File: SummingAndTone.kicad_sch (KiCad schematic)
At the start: 9 parts, among them U2 TL072

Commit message: using smt caps and resistors
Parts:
- C14, C15: footprint ECE319K:C_Axial_200mil -> Capacitor_SMD:C_0805_2012Metric_Pad1.18x1.45mm_HandSolder
- R19, R20, R21, R22, R23: footprint Resistor_THT:R_Axial_DIN0207_L6.3mm_D2.5mm_P10.16mm_Horizontal -> Resistor_SMD:R_0805_2012Metric_Pad1.20x1.40mm_HandSolder
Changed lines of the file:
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@@
 			)
 		)
-		(property "Footprint" "Resistor_THT:R_Axial_DIN0207_L6.3mm_D2.5mm_P10.16mm_Horizontal"
+		(property "Footprint" "Resistor_SMD:R_0805_2012Metric_Pad1.20x1.40mm_HandSolder"
 			(at 133.223 106.68 90)
 			(effects
@@
 			)
 		)
-		(property "Footprint" "Resistor_THT:R_Axial_DIN0207_L6.3mm_D2.5mm_P10.16mm_Horizontal"
+		(property "Footprint" "Resistor_SMD:R_0805_2012Metric_Pad1.20x1.40mm_HandSolder"
 			(at 155.575 121.158 90)
 			(effects
@@
 			)
 		)
-		(property "Footprint" "ECE319K:C_Axial_200mil"
+		(property "Footprint" "Capacitor_SMD:C_0805_2012Metric_Pad1.18x1.45mm_HandSolder"
 			(at 144.78 118.4148 0)
 			(effects
@@
 			)
 		)
-		(property "Footprint" "ECE319K:C_Axial_200mil"
+		(property "Footprint" "Capacitor_SMD:C_0805_2012Metric_Pad1.18x1.45mm_HandSolder"
 			(at 113.665 119.6848 0)
 			(effects
@@
 			)
 		)
-		(property "Footprint" "Resistor_THT:R_Axial_DIN0207_L6.3mm_D2.5mm_P10.16mm_Horizontal"
+		(property "Footprint" "Resistor_SMD:R_0805_2012Metric_Pad1.20x1.40mm_HandSolder"
 			(at 155.575 130.683 90)
 			(effects
@@
 			)
 		)
-		(property "Footprint" "Resistor_THT:R_Axial_DIN0207_L6.3mm_D2.5mm_P10.16mm_Horizontal"
+		(property "Footprint" "Resistor_SMD:R_0805_2012Metric_Pad1.20x1.40mm_HandSolder"
 			(at 139.7 98.933 90)
 			(effects
@@
 			)
 		)
-		(property "Footprint" "Resistor_THT:R_Axial_DIN0207_L6.3mm_D2.5mm_P10.16mm_Horizontal"
+		(property "Footprint" "Resistor_SMD:R_0805_2012Metric_Pad1.20x1.40mm_HandSolder"
 			(at 109.855 111.633 90)
 			(effects

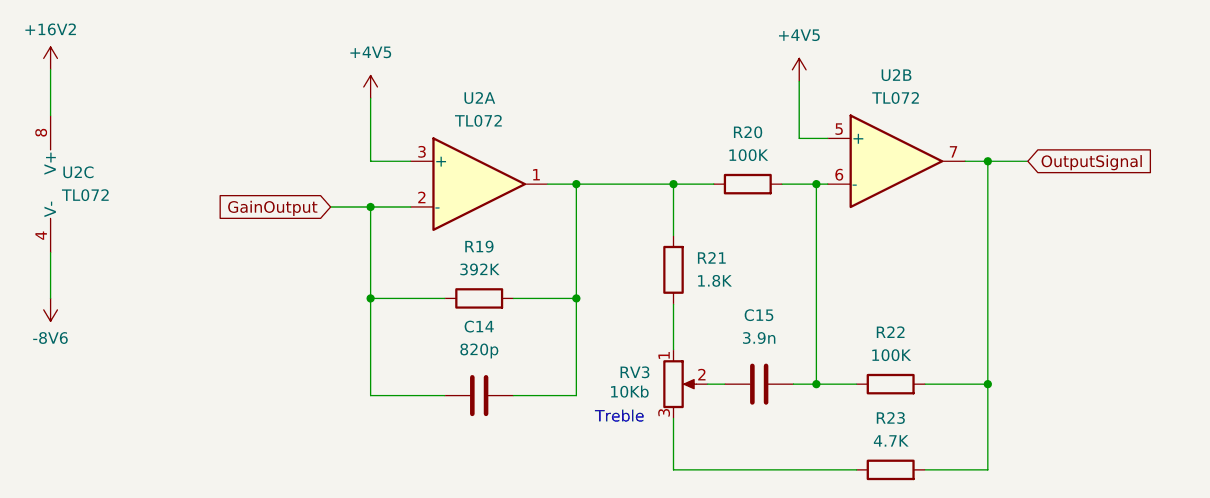
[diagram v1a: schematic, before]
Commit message: change metal film resistor footprint
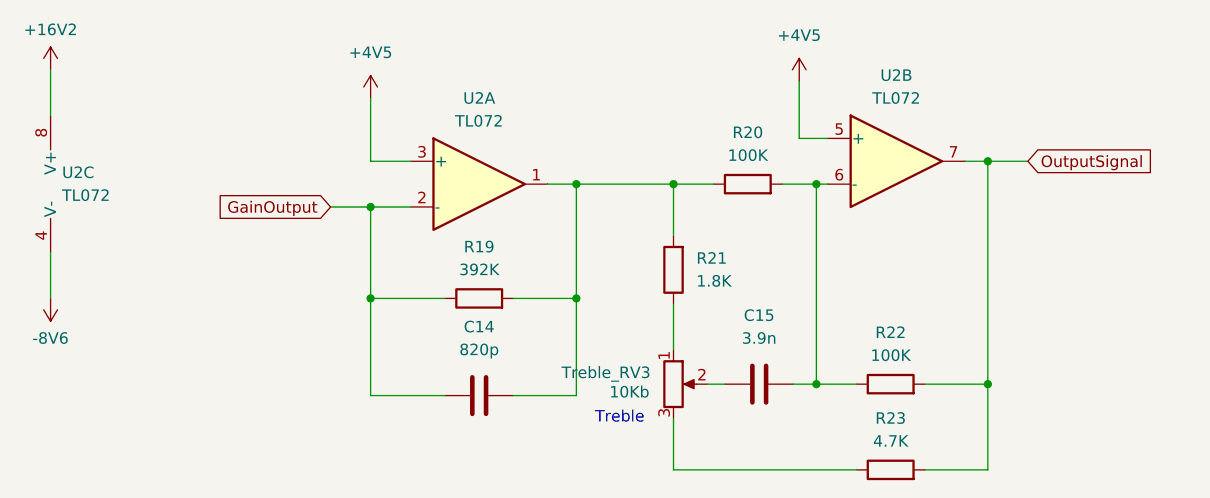
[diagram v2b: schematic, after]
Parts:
- R19: footprint Resistor_SMD:R_0805_2012Metric_Pad1.20x1.40mm_HandSolder -> Resistor_THT:R_Axial_DIN0207_L6.3mm_D2.5mm_P10.16mm_Horizontal
- U2: footprint ECE319K:DIP-8_W7.62mm_LongPads -> Package_SO:SO-8_3.9x4.9mm_P1.27mm
- renumbered RV3 to Treble_RV3
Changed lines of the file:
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@@
 		(on_board yes)
 		(dnp no)
-		(property "Reference" "RV3"
+		(property "Reference" "Treble_RV3"
 			(at 128.905 118.1099 0)
 			(do_not_autoplace yes)
@@
 			(project "KlonePedal"
 				(path "/9e3f79d9-06b6-4799-a8c0-00f1612ca30b/da052ba6-5344-4218-8291-cfab1439bc07"
-					(reference "RV3")
+					(reference "Treble_RV3")
 					(unit 1)
 				)
@@
 			)
 		)
-		(property "Footprint" "ECE319K:DIP-8_W7.62mm_LongPads"
+		(property "Footprint" "Package_SO:SO-8_3.9x4.9mm_P1.27mm"
 			(at 109.855 97.155 0)
 			(effects
@@
 			)
 		)
-		(property "Footprint" "ECE319K:DIP-8_W7.62mm_LongPads"
+		(property "Footprint" "Package_SO:SO-8_3.9x4.9mm_P1.27mm"
 			(at 64.77 97.155 0)
 			(effects
@@
 			)
 		)
-		(property "Footprint" "ECE319K:DIP-8_W7.62mm_LongPads"
+		(property "Footprint" "Package_SO:SO-8_3.9x4.9mm_P1.27mm"
 			(at 156.21 94.615 0)
 			(effects
@@
 			)
 		)
-		(property "Footprint" "Resistor_SMD:R_0805_2012Metric_Pad1.20x1.40mm_HandSolder"
+		(property "Footprint" "Resistor_THT:R_Axial_DIN0207_L6.3mm_D2.5mm_P10.16mm_Horizontal"
 			(at 109.855 111.633 90)
 			(effects

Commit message: add all smd components
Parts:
- R19: footprint Resistor_THT:R_Axial_DIN0207_L6.3mm_D2.5mm_P10.16mm_Horizontal -> Resistor_SMD:R_0805_2012Metric_Pad1.20x1.40mm_HandSolder
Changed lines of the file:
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@@
 			)
 		)
-		(property "Footprint" "Resistor_THT:R_Axial_DIN0207_L6.3mm_D2.5mm_P10.16mm_Horizontal"
+		(property "Footprint" "Resistor_SMD:R_0805_2012Metric_Pad1.20x1.40mm_HandSolder"
 			(at 109.855 111.633 90)
 			(effects
